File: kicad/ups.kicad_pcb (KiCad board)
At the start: 2 copper layers, 47 x 47 mm, 64 parts, among them J1 Input, J2 Output, J3 Batt, J4 CE, J5 NTC, J6 2S_MID, Q1 IRF7324, Q2 AO3401A, Q3 AO3401A, Q4 FDS6890A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

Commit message: Add PCB and Gerbers
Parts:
- added H1: MountingHole_Pad, MountingHole:MountingHole_3.2mm_M3_DIN965_Pad, F.Cu at (97.2, 77.5)
- added H2: MountingHole_Pad, MountingHole:MountingHole_3.2mm_M3_DIN965_Pad, F.Cu at (121.9, 59.1)
- F1: value 5A -> Fuse_Small
- J1: value Input -> VIN
- J4: value CE -> Conn_01x01
- JP1: value CE -> SolderJumper_2_Bridged
- JP2: value GND_STAR -> SolderJumper_2_Bridged; moved to B.Cu
- moved JP2 19.6 mm to (104.1, 71.1), turned to -90 degrees
- moved J4 14.4 mm to (89.5, 88.3)
- moved R12 9.52 mm to (115.6, 88.9)
- moved R18 9.52 mm to (115.6, 84.5)
- moved C20 9.50 mm to (120.4, 86.0), turned to 90 degrees
- moved R7 8.98 mm to (97.8, 54.6), turned to 180 degrees
- moved R1 8.73 mm to (96.5, 70.6)
- moved F1 8.28 mm to (90.2, 55.9)
- moved J1 7.80 mm to (90.1, 49.5), turned to 0 degrees
- moved R3 7.10 mm to (90.8, 71.1), turned to 0 degrees
- moved C19 5.94 mm to (123.7, 81.7), turned to 0 degrees
- moved R10 5.72 mm to (105.4, 88.9)
- moved R11 5.72 mm to (110.5, 88.9)
- moved R16 5.72 mm to (105.4, 84.5), turned to 90 degrees
- moved R17 5.72 mm to (110.5, 84.5)
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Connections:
- C5 pad 1: Net-(Q1A-S1) -> Net-(D2-A)
- C9 pad 2: Net-(Q4B-S2) -> Net-(Q4A-S1)
- D2 pad 1: /ST1 -> Net-(D2-K)
- D3 pad 1: /ST2 -> Net-(D3-K)
- D3 pad 2: Net-(D3-A) -> Net-(D2-A)
- D4 pad 1: /PG -> Net-(D4-K)
- D4 pad 2: Net-(D4-A) -> Net-(D2-A)
- L1 pad 1: Net-(Q4B-S2) -> Net-(Q4A-S1)
- Q1 pad 1: Net-(Q1A-S1) -> Net-(D2-A)
- Q1 pad 3: Net-(Q1A-S1) -> Net-(D2-A)
- Q4 pad 1: Earth -> Net-(Q4A-S1)
- Q4 pad 3: Net-(Q4B-S2) -> Earth
- Q4 pad 5: Net-(J2-Pin_1) -> Net-(Q4A-S1)
- Q4 pad 6: Net-(J2-Pin_1) -> Net-(Q4A-S1)
- Q4 pad 7: Net-(Q4B-S2) -> Net-(J2-Pin_1)
- Q4 pad 8: Net-(Q4B-S2) -> Net-(J2-Pin_1)
- R1 pad 1: Net-(Q1A-S1) -> Net-(D2-A)
- R13 pad 1: Net-(Q1A-S1) -> Net-(D2-K)
- R13 pad 2: Net-(D2-A) -> /ST1
- R14 pad 1: Net-(Q1A-S1) -> Net-(D3-K)
- R14 pad 2: Net-(D3-A) -> /ST2
- R15 pad 1: Net-(Q1A-S1) -> Net-(D4-K)
- R15 pad 2: Net-(D4-A) -> /PG
- R3 pad 1: Net-(Q1A-S1) -> Net-(D2-A)
- U1 pad P19: Net-(Q4A-G1) -> Net-(Q4B-G2)
- U1 pad P20: Net-(Q4B-S2) -> Net-(Q4A-S1)
- U1 pad P21: Net-(Q4B-G2) -> Net-(Q4A-G1)
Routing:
- net Earth: track 0.00 -> 343.4 mm, vias 0 -> 104
- net GND: track 0.00 -> 141.4 mm, vias 0 -> 35
- net Net-(J3-Pin_1): track 0.00 -> 86.6 mm
- net Net-(J2-Pin_1): track 0.00 -> 76.2 mm, vias 0 -> 8
- net Net-(U1-~{BATDRV}): track 0.00 -> 35.4 mm, vias 0 -> 2
- net Net-(JP1-A): track 0.00 -> 34.2 mm, vias 0 -> 2
- net Net-(U1-ACP): track 0.00 -> 31.4 mm
- net Net-(D2-A): track 0.00 -> 30.5 mm
- net /ST2: track 0.00 -> 27.6 mm, vias 0 -> 2
- net Net-(Q4A-S1): track 0.00 -> 26.9 mm
- net /PG: track 0.00 -> 26.3 mm, vias 0 -> 2
- net Net-(J4-Pin_1): track 0.00 -> 25.8 mm, vias 0 -> 2
- net Net-(U1-SRP): track 0.00 -> 25.0 mm
- net /ST1: track 0.00 -> 20.6 mm
- net Net-(J5-Pin_1): track 0.00 -> 20.6 mm
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- added copper zone on B.Cu, net Earth
- added copper zone on F.Cu, net Earth
- added copper zone on B.Cu, net GND
- added copper zone on F.Cu, net GND
- added copper zone on F.Cu, net Net-(J3-Pin_1)
- added copper zone on F.Cu, net Net-(Q4A-S1)
- added copper zone on F.Cu, net Net-(U1-SRP)
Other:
- board size 47 x 47 mm -> 50 x 50 mm
- board text added: "+"
- board text added: "-"
- board text added: "2S_BAL"
- board text added: "BATT"
- board text added: "BQ24610 Low Power UPS"
- board text added: "CE"
- board text added: "CHRG"
- board text added: "CONNECT FIRST"
- board text added: "FULL"
- board text added: "NTC"
- board text added: "PG"
- board text added: "VIN"
- board text added: "VOUT"

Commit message: Minor pcb fix
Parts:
- moved C2 1.50 mm to (102.2, 62.0), turned to 90 degrees
- moved C3 0.56 mm to (103.4, 58.3)
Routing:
- net Net-(J2-Pin_1): track 76.2 -> 77.6 mm
- net GND: track 141.4 -> 142.7 mm, vias 35 -> 36
- added copper zone on F.Cu, net Net-(J2-Pin_1)

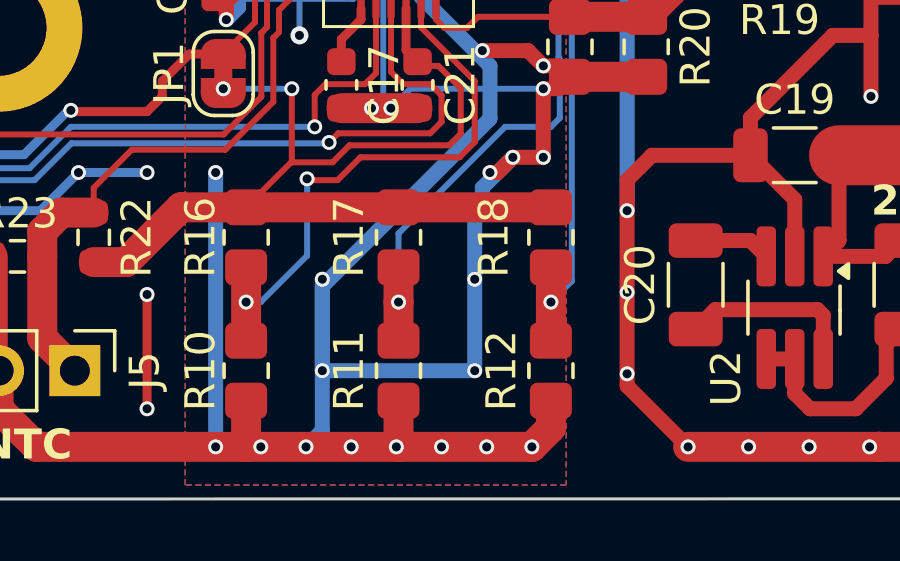
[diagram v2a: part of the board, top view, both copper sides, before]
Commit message: Add ACSET ISETx labels to silkscreen
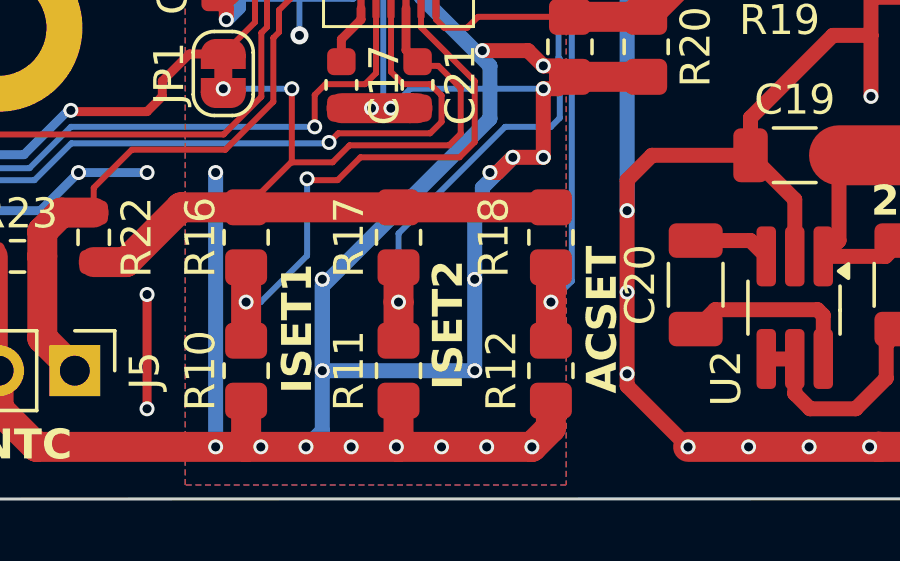
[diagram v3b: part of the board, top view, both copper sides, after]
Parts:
- R11: value 10k -> ISET2
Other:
- board text added: "ACSET"
- board text added: "ISET1"
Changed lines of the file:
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@@
 			)
 		)
-		(property "Value" "10k"
-			(at 0 1.65 -90)
-			(layer "F.Fab")
+		(property "Value" "ISET2"
+			(at 1.524 1.65 270)
+			(layer "F.SilkS")
 			(effects
 				(font
 					(size 1 1)
-					(thickness 0.15)
+					(thickness 0.2)
+					(bold yes)
 				)
 			)
@@
 		)
 	)
+	(gr_text "ISET1"
+		(at 107.696 89.662 90)
+		(layer "F.SilkS")
+		(effects
+			(font
+				(size 1 1)
+				(thickness 0.25)
+				(bold yes)
+			)
+			(justify left bottom)
+		)
+	)
 	(gr_text "-"
 		(at 96.52 46.99 0)
@@
 				(bold yes)
 			)
+			(justify left bottom)
+		)
+	)
+	(gr_text "ACSET"
+		(at 117.856 89.662 90)
+		(layer "F.SilkS")
+		(effects
+			(font
+				(size 1 1)
+				(thickness 0.25)
+				(bold yes)
+			)

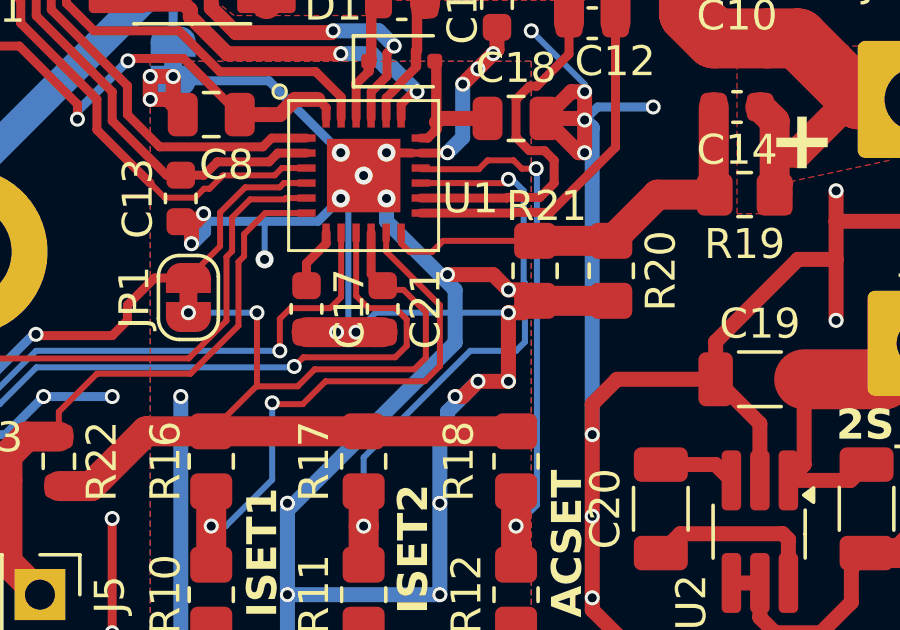
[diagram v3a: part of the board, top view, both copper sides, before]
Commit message: Minor pcb rerouting
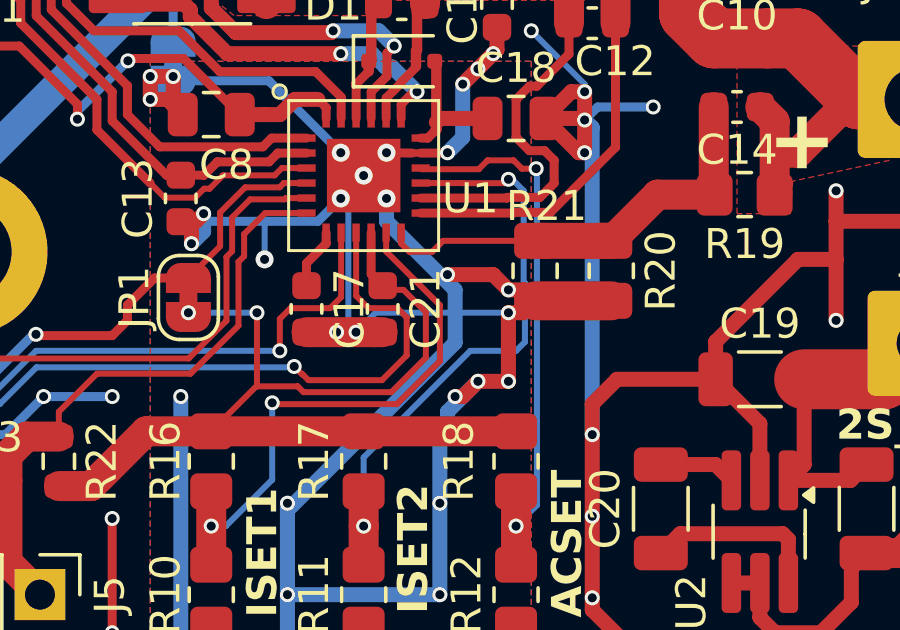
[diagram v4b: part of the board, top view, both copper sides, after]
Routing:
- net /ST2: track 27.6 -> 28.2 mm
